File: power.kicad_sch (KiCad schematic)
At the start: 23 parts, among them U12 BQ24075RGT

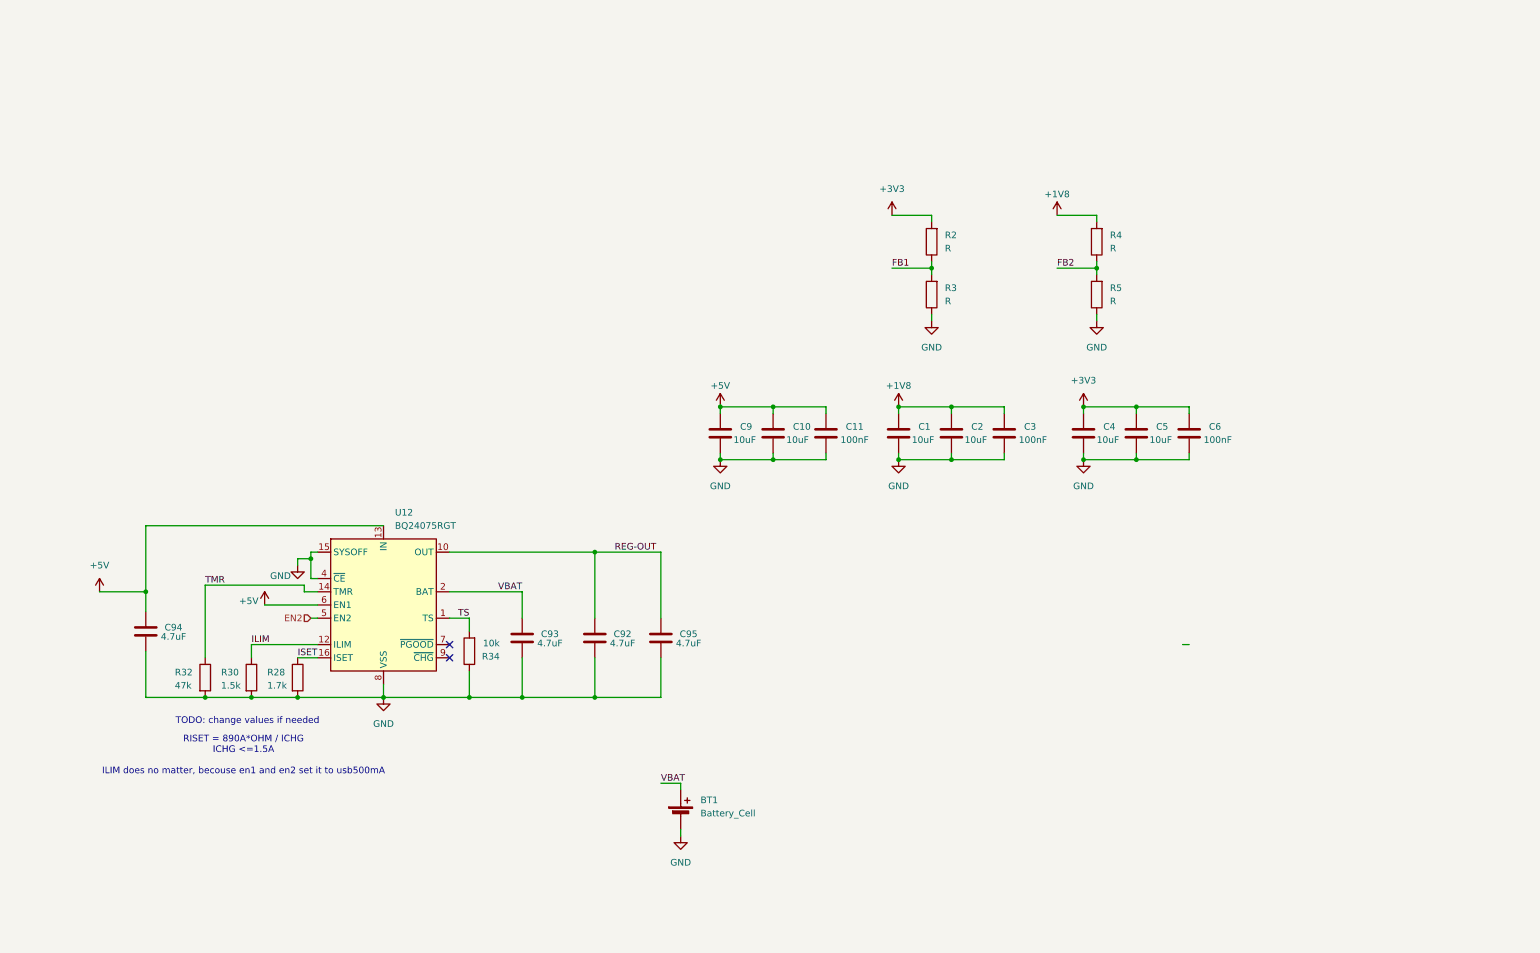
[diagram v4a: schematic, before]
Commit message: re-did power with the new small LDOs and power system
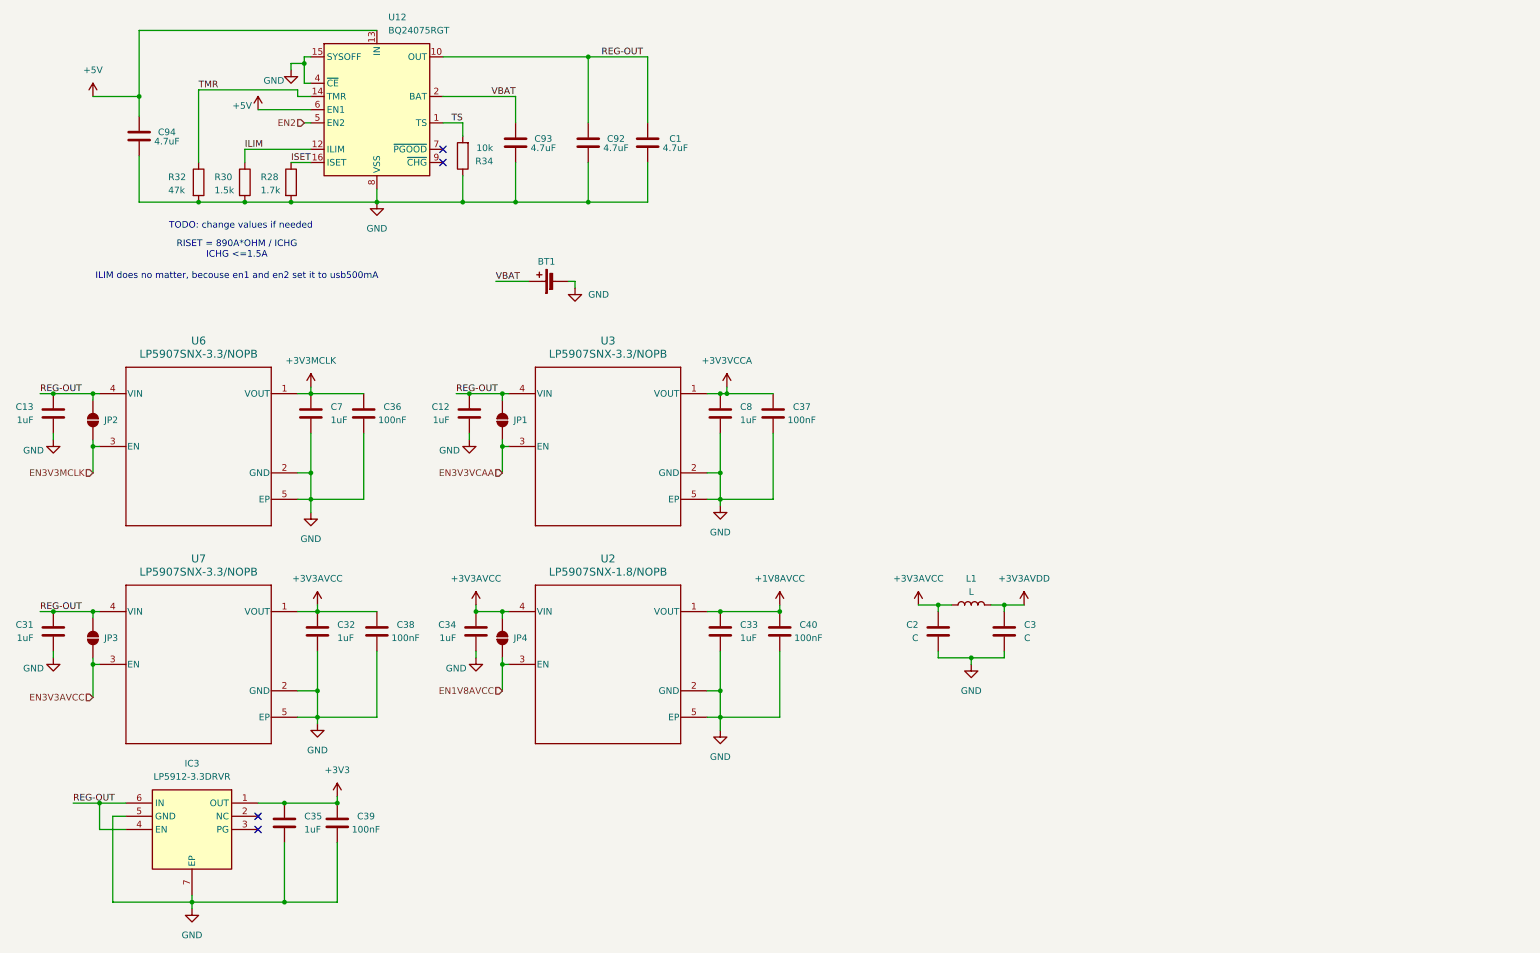
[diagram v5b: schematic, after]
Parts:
- removed C10, C4, C5, C9: 10uF, symbol Device:C
- removed C11, C6: 100nF, symbol Device:C
- removed C95: 4.7uF, Capacitor_SMD:C_0402_1005Metric, symbol Device:C
- removed R2, R3, R4, R5: R, symbol Device:R
- added C12, C13, C31, C32, C33, C34, C35, C7, C8: 1uF, symbol Device:C
- added C36, C37, C38, C39, C40: 100nF, symbol Device:C
- added IC3: LP5912-3.3DRVR, SON65P200X200X80-7N, symbol LP5912-3_3DRVR:LP5912-3.3DRVR
- added JP1, JP2, JP3, JP4: SolderJumper_2_Open, Jumper:SolderJumper-2_P1.3mm_Open_RoundedPad1.0x1.5mm, symbol Jumper:SolderJumper_2_Open
- added L1: L, symbol Device:L
- added U2: LP5907SNX-1.8/NOPB, Package_SON:Texas_X2SON-4_1x1mm_P0.65mm, symbol LP5907SNX-1-8-NOPB:LP5907SNX-1.8_NOPB
- added U3, U6, U7: LP5907SNX-3.3/NOPB, Package_SON:Texas_X2SON-4_1x1mm_P0.65mm, symbol LP5907SNX-3-3-NOPB:LP5907SNX-3.3_NOPB
- C1: value 10uF -> 4.7uF; footprint (none) -> Capacitor_SMD:C_0402_1005Metric; LCSC (none) -> C307423
- C2: value 10uF -> C
- C3: value 100nF -> C
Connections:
- net +3V3: now also C35.1, C39.1, IC3.1 (OUT)
- net GND: now also C1.1, C12.2, C13.2, C31.2, C32.2, C33.2, C34.2, C35.2, C36.2, C37.2, C38.2, C39.2, C40.2, C7.2, C8.2, IC3.5 (GND), IC3.7 (EP), U2.2 (GND), U2.5 (EP), U3.2 (GND), U3.5 (EP), U6.2 (GND), U6.5 (EP), U7.2 (GND), U7.5 (EP); no longer C1.2
- net REG-OUT: now also C1.2, C12.1, C13.1, C31.1, IC3.4 (EN), IC3.6 (IN), JP1.2 (B), JP2.2 (B), JP3.2 (B), U3.4 (VIN), U6.4 (VIN), U7.4 (VIN)
- removed net +1V8: C1.1, C2.1, C3.1
- new net +1V8AVCC: C33.1, C40.1, U2.1 (VOUT)
- new net +3V3AVCC: C2.1, C32.1, C34.1, C38.1, JP4.2 (B), L1.1, U2.4 (VIN), U7.1 (VOUT)
- new net +3V3AVDD: C3.1, L1.2
- new net +3V3MCLK: C36.1, C7.1, U6.1 (VOUT)
- new net +3V3VCCA: C37.1, C8.1, U3.1 (VOUT)
- new net EN1V8AVCC: JP4.1 (A), U2.3 (EN)
- new net EN3V3AVCC: JP3.1 (A), U7.3 (EN)
- new net EN3V3MCLK: JP2.1 (A), U6.3 (EN)
- new net EN3V3VCAA: JP1.1 (A), U3.3 (EN)
- no-connect marks 2 -> 4
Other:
- moved on the sheet: BT1, C92, C93, C94, R28, R30, R32, R34, U12

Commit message: i2c, i2s, uart, en, sd card
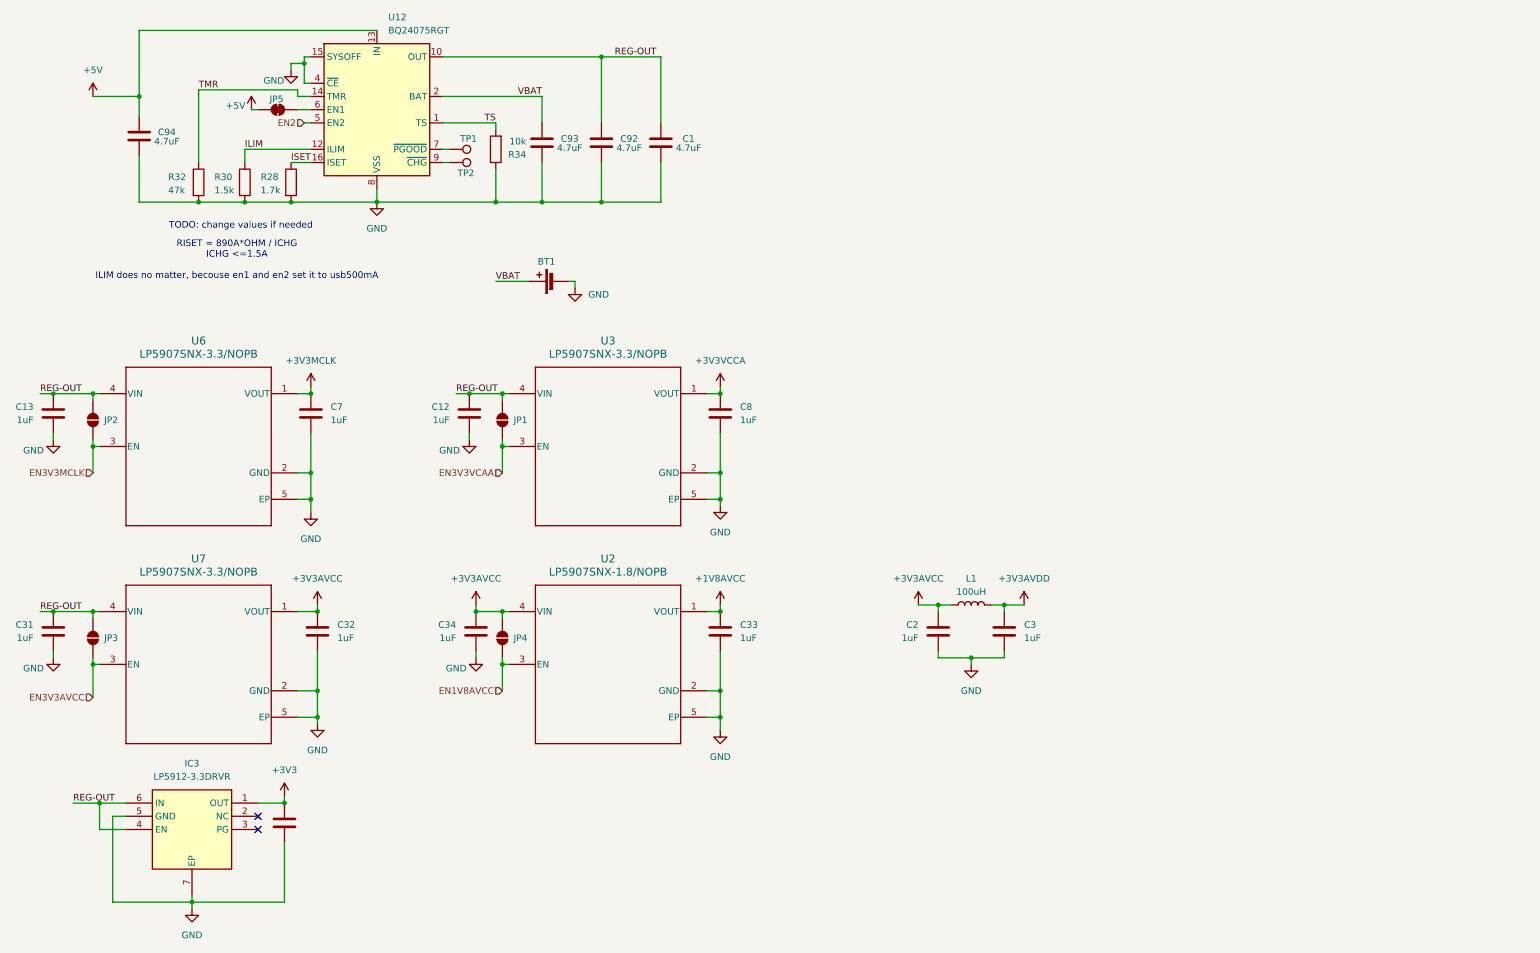
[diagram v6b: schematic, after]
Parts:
- removed C36, C37, C38, C39, C40: 100nF, symbol Device:C
- added JP5: SolderJumper_2_Bridged, Jumper:SolderJumper-2_P1.3mm_Bridged_RoundedPad1.0x1.5mm, symbol Jumper:SolderJumper_2_Bridged
- added TP1, TP2: TestPoint, TestPoint:TestPoint_Pad_D1.5mm, symbol Connector:TestPoint
- C2, C3: value C -> 1uF
- L1: value L -> 100uH; footprint (none) -> Inductor_SMD:L_TDK_MLZ2012_h1.25mm
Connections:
- net +5V: now also JP5.1 (A); no longer U12.6 (EN1)
- net at U12.7 (~{PGOOD}): now also TP1.1
- net at U12.9 (~{CHG}): now also TP2.1
- new net: JP5.2 (B), U12.6 (EN1)
- no-connect marks 4 -> 2
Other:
- moved on the sheet: C1, C92, C93, R34

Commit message: finishing up schematic
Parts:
- removed JP1, JP2, JP3, JP4: SolderJumper_2_Open, Jumper:SolderJumper-2_P1.3mm_Open_RoundedPad1.0x1.5mm, symbol Jumper:SolderJumper_2_Open
- added JP1, JP2, JP3, JP4: SolderJumper_2_Bridged, Jumper:SolderJumper-2_P1.3mm_Bridged_RoundedPad1.0x1.5mm, symbol Jumper:SolderJumper_2_Bridged
- added R21: 10k, symbol Device:R
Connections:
- net +3V3AVCC: now also JP4.2 (B)
- net EN1V8AVCC: now also JP4.1 (A)
- net EN2: now also R21.1
- net EN3V3AVCC: now also JP3.1 (A)
- net EN3V3MCLK: now also JP2.1 (A)
- net EN3V3VCAA: now also JP1.1 (A)
- net GND: now also R21.2
- net REG-OUT: now also JP1.2 (B), JP2.2 (B), JP3.2 (B)
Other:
- moved on the sheet: BT1, C94, R28, R30, R32

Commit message: esd, jack, io expander, led, power swquence
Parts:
- removed JP2, JP3, JP4: SolderJumper_2_Bridged, Jumper:SolderJumper-2_P1.3mm_Bridged_RoundedPad1.0x1.5mm, symbol Jumper:SolderJumper_2_Bridged
- added C28, C51: 1uF, symbol Device:C
- added JP10, JP2, JP3: SolderJumper_2_Open, Jumper:SolderJumper-2_P1.3mm_Open_RoundedPad1.0x1.5mm, symbol Jumper:SolderJumper_2_Open
- added U4: LP5907SNX-1.8/NOPB, Package_SON:Texas_X2SON-4_1x1mm_P0.65mm, symbol LP5907SNX-1-8-NOPB:LP5907SNX-1.8_NOPB
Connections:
- net +3V3: now also C2.1, L1.1
- net +3V3AVCC: now also C28.1, JP3.1 (A), U4.3 (EN), U4.4 (VIN); no longer C2.1, L1.1
- net EN1V8AVCC: now also JP3.2 (B)
- net EN3V3AVCC: now also JP2.2 (B)
- net EN3V3MCLK: now also JP1.1 (A)
- net EN3V3VCAA: now also JP10.2 (B); no longer JP1.1 (A)
- net GND: now also C28.2, C51.2, U4.2 (GND), U4.5 (EP)
- net REG-OUT: now also JP10.1 (A), JP2.1 (A)
- new net +1V8MIC: C51.1, U4.1 (VOUT)
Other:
- moved on the sheet: JP1
